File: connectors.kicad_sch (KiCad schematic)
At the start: 47 parts, among them CN901 HuCARD, CN902 JOY1

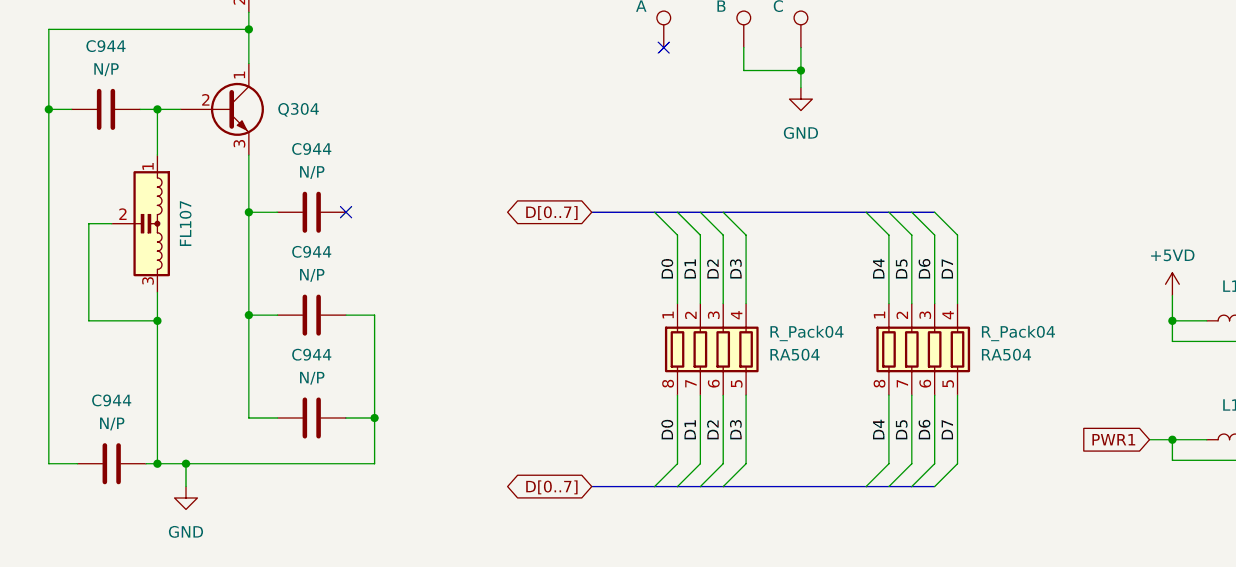
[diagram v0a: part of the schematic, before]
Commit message: Add more capacitor values, rearrange some schematics.
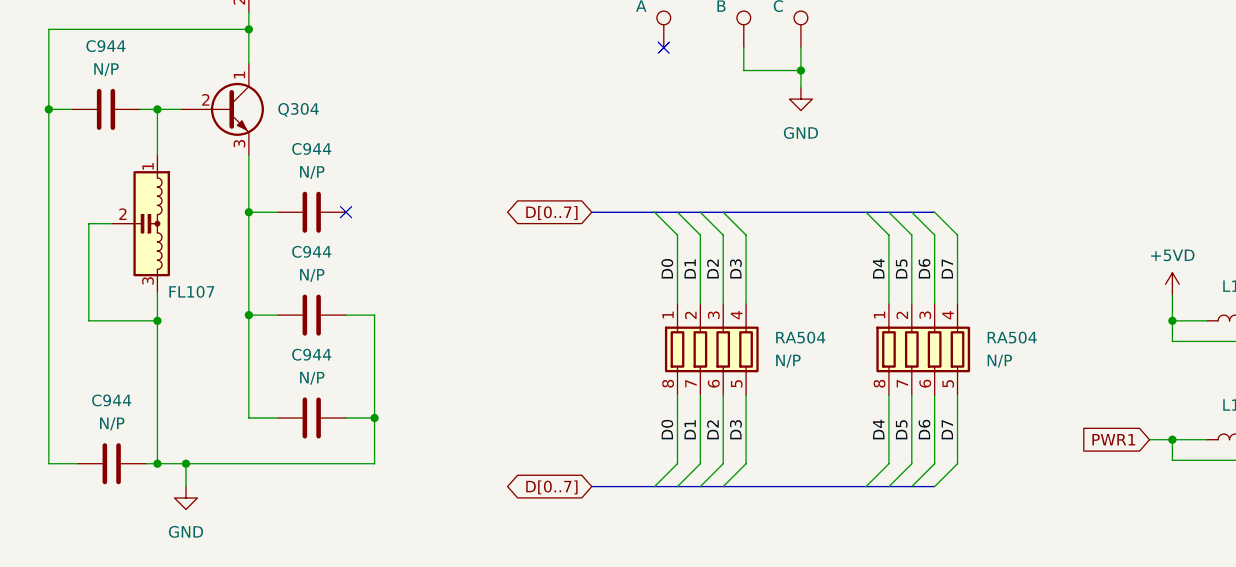
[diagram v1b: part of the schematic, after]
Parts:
- RA504: value R_Pack04 -> N/P
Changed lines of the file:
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@@
   (symbol (lib_id "Device:R_Pack04") (at 185.42 197.485 0) (mirror x) (unit 1)
     (in_bom yes) (on_board yes) (dnp no)
-    (property "Reference" "RA504" (at 190.5 198.12 0)
+    (property "Reference" "RA504" (at 191.135 196.215 0)
       (effects (font (size 1.27 1.27)) (justify left))
     )
-    (property "Value" "R_Pack04" (at 190.5 195.58 0)
+    (property "Value" "N/P" (at 191.135 198.755 0)
       (effects (font (size 1.27 1.27)) (justify left))
     )
@@
   (symbol (lib_id "Device:R_Pack04") (at 208.915 197.485 0) (mirror x) (unit 1)
     (in_bom yes) (on_board yes) (dnp no)
-    (property "Reference" "RA504" (at 213.995 198.12 0)
+    (property "Reference" "RA504" (at 214.63 196.215 0)
       (effects (font (size 1.27 1.27)) (justify left))
     )
-    (property "Value" "R_Pack04" (at 213.995 195.58 0)
+    (property "Value" "N/P" (at 214.63 198.755 0)
       (effects (font (size 1.27 1.27)) (justify left))
     )
@@
   (symbol (lib_id "Device:Filter_EMI_LCL") (at 120.015 183.515 270) (unit 1)
     (in_bom yes) (on_board yes) (dnp no)
-    (property "Reference" "FL107" (at 125.73 183.515 0)
-      (effects (font (size 1.27 1.27)))
-    )
+    (property "Reference" "FL107" (at 126.365 191.135 90)
+      (effects (font (size 1.27 1.27)))
+    )

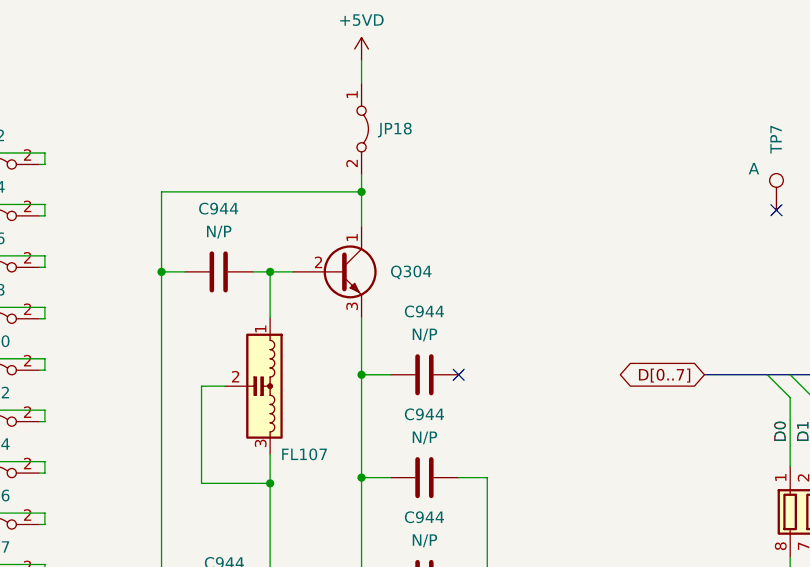
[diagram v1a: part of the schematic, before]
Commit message: Add markings for SMD Ds and Qs.
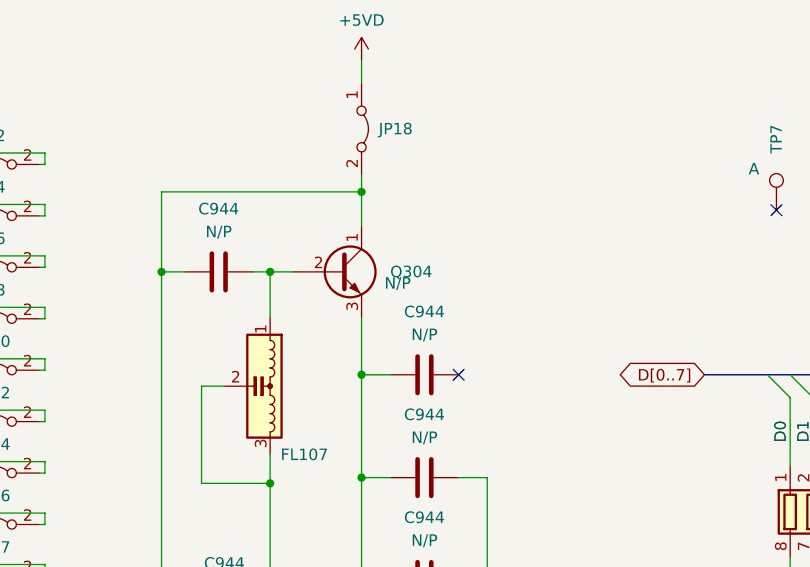
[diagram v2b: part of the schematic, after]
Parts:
- Q304: value ~ -> N/P
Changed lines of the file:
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@@
       (effects (font (size 1.27 1.27)) (justify left))
     )
-    (property "Value" "~" (at 135.255 172.085 0)
+    (property "Value" "N/P" (at 135.255 172.085 0)
       (effects (font (size 1.27 1.27)) (justify left))
     )

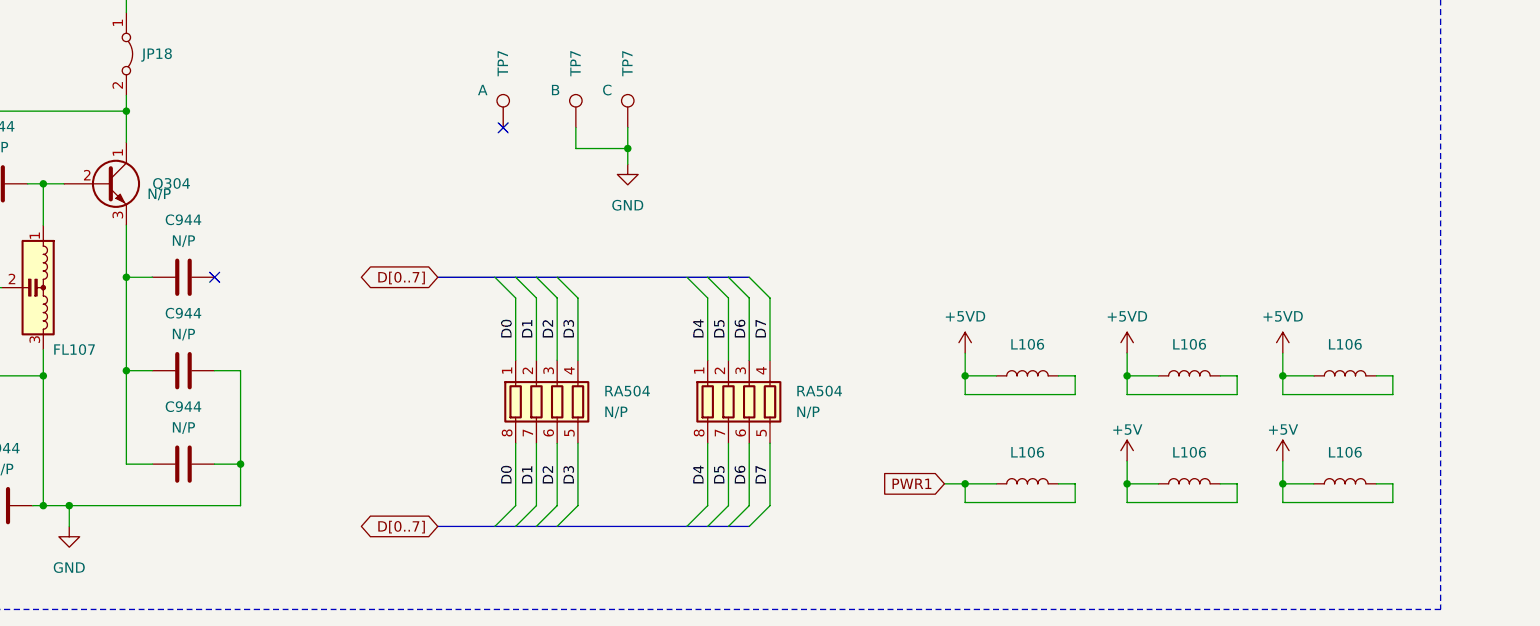
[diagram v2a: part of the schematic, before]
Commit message: More schematic clean-up/annotation.
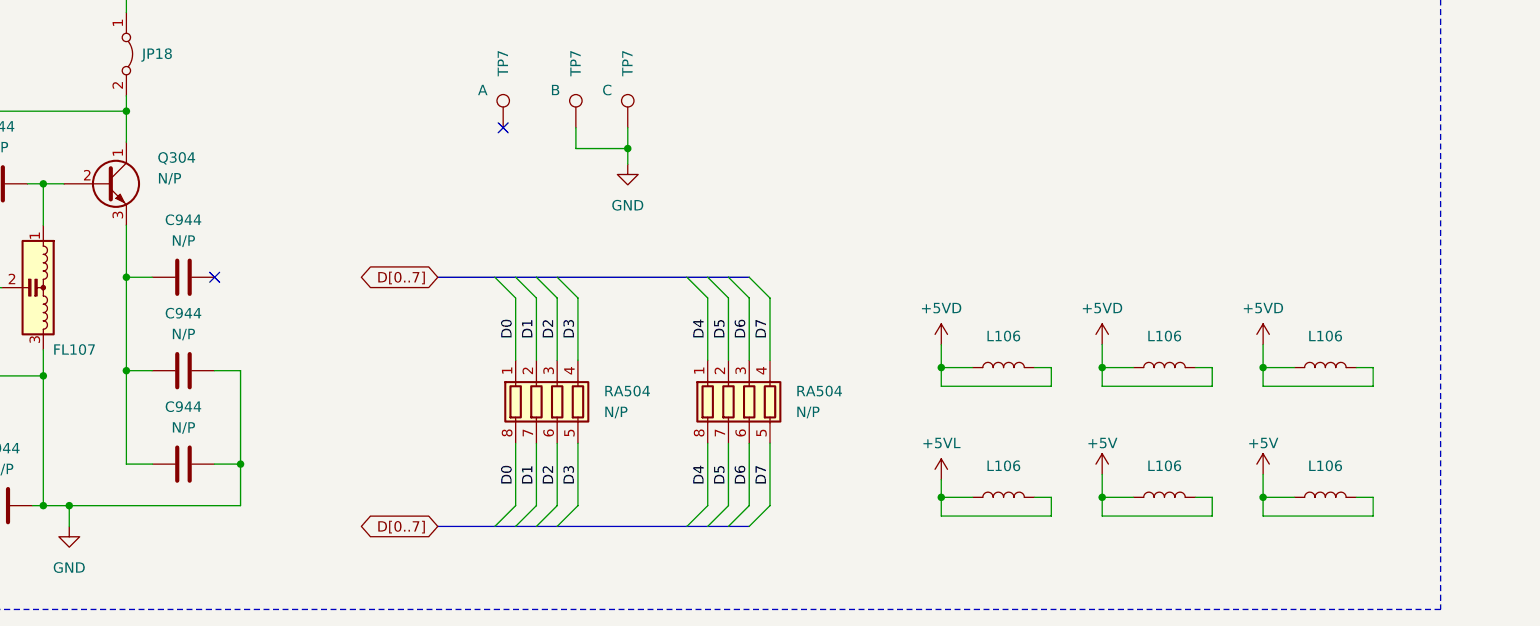
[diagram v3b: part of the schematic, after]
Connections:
- net PWR1 renamed +5VL
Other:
- company: (none) -> By Cosam
- title: PC Engine Connectors -> PC Engine Duo Connectors
- moved on the sheet: L106

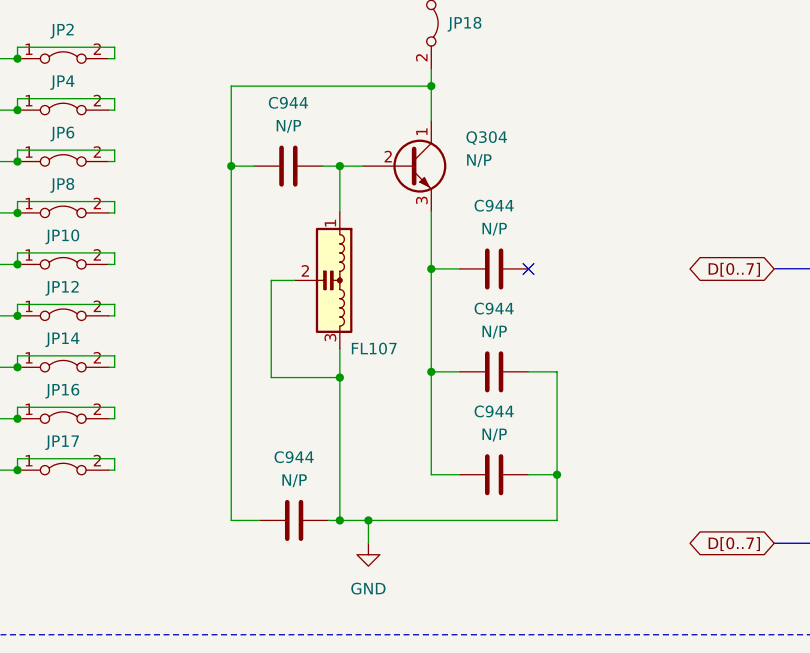
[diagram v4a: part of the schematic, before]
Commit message: Minor schematic/silkscreen changes.
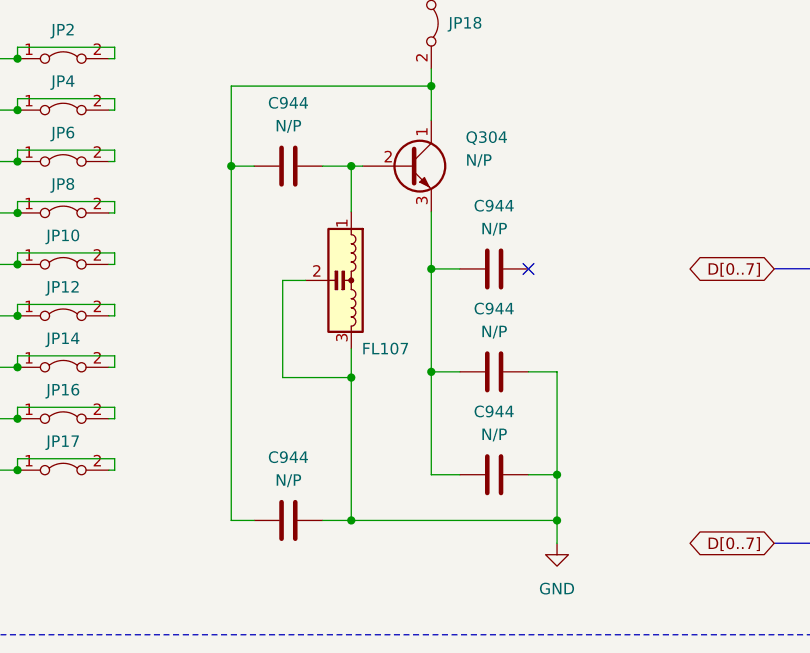
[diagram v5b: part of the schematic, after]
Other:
- moved on the sheet: C944, FL107
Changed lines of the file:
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@@
   (junction (at 132.715 182.245) (diameter 0) (color 0 0 0 0)
   )
-  (junction (at 125.73 210.185) (diameter 0) (color 0 0 0 0)
-  )
   (junction (at 132.715 193.675) (diameter 0) (color 0 0 0 0)
   )
   (junction (at 70.231 187.452) (diameter 0) (color 0 0 0 0)
   )
+  (junction (at 146.685 210.185) (diameter 0) (color 0 0 0 0)
+  )
   (junction (at 273.685 76.2) (diameter 0) (color 0 0 0 0)
   )
@@
   (junction (at 86.741 204.597) (diameter 0) (color 0 0 0 0)
   )
-  (junction (at 122.555 210.185) (diameter 0) (color 0 0 0 0)
-  )
   (junction (at 80.391 198.882) (diameter 0) (color 0 0 0 0)
   )
@@
   (junction (at 80.391 193.167) (diameter 0) (color 0 0 0 0)
   )
-  (junction (at 122.555 170.815) (diameter 0) (color 0 0 0 0)
-  )
-  (junction (at 122.555 194.31) (diameter 0) (color 0 0 0 0)
+  (junction (at 123.825 170.815) (diameter 0) (color 0 0 0 0)
+  )
+  (junction (at 123.825 194.31) (diameter 0) (color 0 0 0 0)
   )
   (junction (at 86.741 198.882) (diameter 0) (color 0 0 0 0)
   )
   (junction (at 86.741 176.022) (diameter 0) (color 0 0 0 0)
+  )
+  (junction (at 123.825 210.185) (diameter 0) (color 0 0 0 0)
   )
   (junction (at 86.741 164.592) (diameter 0) (color 0 0 0 0)
@@
     (stroke (width 0) (type default))
   )
-  (wire (pts (xy 125.73 210.185) (xy 125.73 212.725))
+  (wire (pts (xy 146.685 210.185) (xy 146.685 212.725))
     (stroke (width 0) (type default))
   )
@@
     (stroke (width 0) (type default))
   )
-  (wire (pts (xy 122.555 170.815) (xy 125.095 170.815))
+  (wire (pts (xy 120.65 170.815) (xy 123.825 170.815))
     (stroke (width 0) (type default))
   )
@@
     (stroke (width 0) (type default))
   )
+  (wire (pts (xy 123.825 210.185) (xy 146.685 210.185))
+    (stroke (width 0) (type default))
+  )
   (wire (pts (xy 219.71 53.34) (xy 219.71 59.69))
     (stroke (width 0) (type default))
@@
     (stroke (width 0) (type default))
   )
+  (wire (pts (xy 120.65 210.185) (xy 123.825 210.185))
+    (stroke (width 0) (type default))
+  )
   (wire (pts (xy 234.95 59.69) (xy 232.41 59.69))
     (stroke (width 0) (type default))
@@
     (stroke (width 0) (type default))
   )
-  (wire (pts (xy 121.285 210.185) (xy 122.555 210.185))
-    (stroke (width 0) (type default))
-  )
   (bus (pts (xy 58.166 184.912) (xy 58.166 179.197))
     (stroke (width 0) (type default))
@@
     (stroke (width 0) (type default))
   )
-  (wire (pts (xy 122.555 210.185) (xy 125.73 210.185))
-    (stroke (width 0) (type default))
-  )
   (wire (pts (xy 81.28 92.71) (xy 82.55 92.71))
     (stroke (width 0) (type default))
@@
     (stroke (width 0) (type default))
   )
-  (wire (pts (xy 117.475 183.515) (xy 114.935 183.515))
+  (wire (pts (xy 118.745 183.515) (xy 116.205 183.515))
     (stroke (width 0) (type default))
   )
@@
     (stroke (width 0) (type default))
   )
-  (wire (pts (xy 122.555 194.31) (xy 122.555 210.185))
+  (wire (pts (xy 123.825 194.31) (xy 123.825 210.185))
     (stroke (width 0) (type default))
   )
@@
     (stroke (width 0) (type default))
   )
-  (wire (pts (xy 114.935 183.515) (xy 114.935 194.31))
+  (wire (pts (xy 116.205 183.515) (xy 116.205 194.31))
     (stroke (width 0) (type default))
   )
@@
     (stroke (width 0) (type default))
   )
-  (wire (pts (xy 120.65 170.815) (xy 122.555 170.815))
-    (stroke (width 0) (type default))
-  )
   (wire (pts (xy 97.536 158.877) (xy 96.901 158.877))
     (stroke (width 0) (type default))
@@
     (stroke (width 0) (type default))
   )
+  (wire (pts (xy 123.825 170.815) (xy 125.095 170.815))
+    (stroke (width 0) (type default))
+  )
   (wire (pts (xy 81.28 72.39) (xy 103.505 72.39))
     (stroke (width 0) (type default))
@@
     (stroke (width 0) (type default))
   )
-  (wire (pts (xy 146.685 210.185) (xy 125.73 210.185))
-    (stroke (width 0) (type default))
-  )
   (wire (pts (xy 146.812 62.484) (xy 150.622 62.484))
     (stroke (width 0) (type default))
@@
     (stroke (width 0) (type default))
   )
-  (wire (pts (xy 122.555 170.815) (xy 122.555 175.895))
+  (wire (pts (xy 123.825 170.815) (xy 123.825 175.895))
     (stroke (width 0) (type default))
   )
@@
     (stroke (width 0) (type default))
   )
-  (wire (pts (xy 114.935 194.31) (xy 122.555 194.31))
+  (wire (pts (xy 116.205 194.31) (xy 123.825 194.31))
     (stroke (width 0) (type default))
   )
@@
     (stroke (width 0) (type default))
   )
-  (wire (pts (xy 122.555 194.31) (xy 122.555 191.135))
+  (wire (pts (xy 123.825 194.31) (xy 123.825 191.135))
     (stroke (width 0) (type default))
   )
@@
     (stroke (width 0) (type default))
   )
-  (wire (pts (xy 110.49 210.185) (xy 113.665 210.185))
+  (wire (pts (xy 110.49 210.185) (xy 113.03 210.185))
     (stroke (width 0) (type default))
   )
@@
     )
   )
-  (symbol (lib_id "Device:C") (at 117.475 210.185 90) (unit 1)
+  (symbol (lib_id "Device:C") (at 116.84 210.185 90) (unit 1)
     (in_bom yes) (on_board yes) (dnp no) (fields_autoplaced)
-    (property "Reference" "C944" (at 117.475 203.2 90)
-      (effects (font (size 1.27 1.27)))
-    )
-    (property "Value" "N/P" (at 117.475 205.74 90)
-      (effects (font (size 1.27 1.27)))
-    )
-    (property "Footprint" "A-PCENGINE:SMD_0805_Narrow_NoSilk" (at 121.285 209.2198 0)
-      (effects (font (size 1.27 1.27)) hide)
-    )
-    (property "Datasheet" "~" (at 117.475 210.185 0)
+    (property "Reference" "C944" (at 116.84 203.2 90)
+      (effects (font (size 1.27 1.27)))
+    )
+    (property "Value" "N/P" (at 116.84 205.74 90)
+      (effects (font (size 1.27 1.27)))
+    )
+    (property "Footprint" "A-PCENGINE:SMD_0805_Narrow_NoSilk" (at 120.65 209.2198 0)
+      (effects (font (size 1.27 1.27)) hide)
+    )
+    (property "Datasheet" "~" (at 116.84 210.185 0)
       (effects (font (size 1.27 1.27)) hide)
     )
@@
     )
   )
-  (symbol (lib_id "power:GND") (at 125.73 212.725 0) (unit 1)
+  (symbol (lib_id "power:GND") (at 146.685 212.725 0) (unit 1)
     (in_bom yes) (on_board yes) (dnp no) (fields_autoplaced)
-    (property "Reference" "#PWR0138" (at 125.73 219.075 0)
-      (effects (font (size 1.27 1.27)) hide)
-    )
-    (property "Value" "GND" (at 125.73 217.805 0)
-      (effects (font (size 1.27 1.27)))
-    )
-    (property "Footprint" "" (at 125.73 212.725 0)
-      (effects (font (size 1.27 1.27)) hide)
-    )
-    (property "Datasheet" "" (at 125.73 212.725 0)
+    (property "Reference" "#PWR0138" (at 146.685 219.075 0)
+      (effects (font (size 1.27 1.27)) hide)
+    )
+    (property "Value" "GND" (at 146.685 217.805 0)
+      (effects (font (size 1.27 1.27)))
+    )
+    (property "Footprint" "" (at 146.685 212.725 0)
+      (effects (font (size 1.27 1.27)) hide)
+    )
+    (property "Datasheet" "" (at 146.685 212.725 0)
       (effects (font (size 1.27 1.27)) hide)
     )
@@
     )
   )
-  (symbol (lib_id "Device:Filter_EMI_LCL") (at 120.015 183.515 270) (unit 1)
+  (symbol (lib_id "Device:Filter_EMI_LCL") (at 121.285 183.515 270) (unit 1)
     (in_bom yes) (on_board yes) (dnp no)
-    (property "Reference" "FL107" (at 126.365 191.135 90)
-      (effects (font (size 1.27 1.27)))
-    )
-    (property "Value" "Filter_EMI_LCL" (at 125.095 183.515 0)
-      (effects (font (size 1.27 1.27)) hide)
-    )
-    (property "Footprint" "A-PCENGINE:FL-5.00mm_NoSilk" (at 120.015 183.515 90)
-      (effects (font (size 1.27 1.27)) hide)
-    )
-    (property "Datasheet" "" (at 120.015 183.515 90)
-      (effects (font (size 1.27 1.27)) hide)
-    )
+    (property "Reference" "FL107" (at 127.635 191.135 90)
+      (effects (font (size 1.27 1.27)))
+    )
+    (property "Value" "Filter_EMI_LCL" (at 126.365 183.515 0)
+      (effects (font (size 1.27 1.27)) hide)
+    )
+    (property "Footprint" "A-PCENGINE:FL-5.00mm_NoSilk" (at 121.285 183.515 90)
+      (effects (font (size 1.27 1.27)) hide)
+    )
+    (property "Datasheet" "" (at 121.285 183.515 90)
+      (effects (font (size 1.27 1.27)) hide)
+    )
